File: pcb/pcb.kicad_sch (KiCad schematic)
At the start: 0 parts

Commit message: worked on buttons design
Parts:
- added CH1: choc_v1_SW_HS, PCM_marbastlib-choc:SW_choc_v1_HS_CPG135001S30_1u, symbol PCM_marbastlib-choc:choc_v1_SW_HS_CPG135001S30
- added D1: 1N4148, PCM_Diode_THT_AKL:D_DO-35_SOD27_P7.62mm_Horizontal, symbol PCM_Diode_AKL:1N4148
- added J1: PINHD_1x5_Female, PCM_4ms_Connector:Pins_1x05_2.54mm_TH, symbol PCM_SL_Pin_Headers:PINHD_1x5_Female
- added LED1: choc_SK6812MINI-E, PCM_marbastlib-choc:LED_choc_6028R, symbol PCM_marbastlib-choc:choc_SK6812MINI-E
- added R1: 500, Resistor_THT:R_Axial_DIN0207_L6.3mm_D2.5mm_P10.16mm_Horizontal, symbol PCM_SL_Resistors:Resistor
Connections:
- new net: LED1.2 (DOUT), R1.1
- new net: J1.5, R1.2
- new net: D1.1 (K), J1.2
- new net: CH1.1, D1.2 (A)
- new net: CH1.2, J1.1, LED1.1 (VDD)
- new net: J1.3, LED1.4 (VSS)
- new net: J1.4, LED1.3 (DIN)

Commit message: topshefl work
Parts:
- R1: footprint Resistor_THT:R_Axial_DIN0207_L6.3mm_D2.5mm_P10.16mm_Horizontal -> PCM_4ms_Resistor:R_0603
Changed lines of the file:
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@@
 			)
 		)
-		(property "Footprint" "Resistor_THT:R_Axial_DIN0207_L6.3mm_D2.5mm_P10.16mm_Horizontal"
+		(property "Footprint" "PCM_4ms_Resistor:R_0603"
 			(at 109.601 59.182 0)
 			(effects

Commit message: huh
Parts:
- removed D1: 1N4148, PCM_Diode_THT_AKL:D_DO-35_SOD27_P7.62mm_Horizontal, symbol PCM_Diode_AKL:1N4148
- removed J1: PINHD_1x5_Female, PCM_4ms_Connector:Pins_1x05_2.54mm_TH, symbol PCM_SL_Pin_Headers:PINHD_1x5_Female
- removed LED1: choc_SK6812MINI-E, PCM_marbastlib-choc:LED_choc_6028R, symbol PCM_marbastlib-choc:choc_SK6812MINI-E
- removed R1: 500, PCM_4ms_Resistor:R_0603, symbol PCM_SL_Resistors:Resistor

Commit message: some schematic changes
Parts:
- added C1: 10uF, PCM_Capacitor_SMD_Handsoldering_AKL:C_0805_2012Metric, symbol PCM_Capacitor_AKL:C_0402
- added C2, C4, C5: 100uF, PCM_Capacitor_SMD_Handsoldering_AKL:C_0805_2012Metric, symbol PCM_Capacitor_AKL:C_0402
- added C3: 1uF, PCM_Capacitor_SMD_Handsoldering_AKL:C_0805_2012Metric, symbol PCM_Capacitor_AKL:C_0402
- added IC1: LD1117-3.3V-SOT223, 4ms_Package_SOT:SOT223, symbol PCM_4ms_Regulator:LD1117-3.3V-SOT223
- added J1: Input, PCM_SparkFun-Connector:JST_1x08_P1.25mm_Locking_Horizontal_SMD, symbol PCM_SparkFun-Connector:Conn_01x08_JST_P1.25mm_Locking_Horizontal_SMD
- added J2: Output, PCM_SparkFun-Connector:JST_1x08_P1.25mm_Locking_Horizontal_SMD, symbol PCM_SparkFun-Connector:Conn_01x08_JST_P1.25mm_Locking_Horizontal_SMD
- added J3: PinHeader_01x05_P2.54mm_Horizontal_SMD, PCM_fab:PinHeader_01x05_P2.54mm_Horizontal_SMD, symbol PCM_fab:PinHeader_01x05_P2.54mm_Horizontal_SMD
- added JMP_BTN1, JMP_BTN2, JMP_BTN3, JMP_BTN4, JMP_BTN5, JMP_BTN6, JMP_BTN7, JMP_BTN8: ~, PCM_SparkFun-Jumper:Jumper_2_NO_NoSilk, symbol PCM_SparkFun-Jumper:SolderJumper_2_Open_No_Silk
- added R1: 10k, PCM_4ms_LED:LED_3mm_C1A2_Polarity_Indicator, symbol PCM_Resistor_US_AKL:R_0805
- added R2, R3: 22, PCM_Resistor_SMD_AKL:R_0805_2012Metric, symbol PCM_Resistor_US_AKL:R_0805
- added SW1: Push_Button, Button_Switch_THT:SW_PUSH_6mm, symbol PCM_SL_Devices:Push_Button
- added U1: ~, symbol mycustomsymbols:STM32F042K6
- added USB1: HRO-TYPE-C-31-M-12, extern:HRO-TYPE-C-31-M-12-HandSoldering, symbol Type-C:HRO-TYPE-C-31-M-12
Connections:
- net +3.3V: now reaches CH1.1
- net +3.3V: now also C1.2, C2.2, C4.2, C5.2, IC1.2 (OUT), J1.1 (Pin_1), J2.1 (Pin_1), J3.5 (Pin_5), SW1.2, U1.1 (VDD), U1.17 (VDDIO2), U1.5 (VDDA)
- net at CH1.2: now also JMP_BTN1.1 (A), JMP_BTN2.2 (B), JMP_BTN3.2 (B), JMP_BTN4.2 (B), JMP_BTN5.2 (B), JMP_BTN6.2 (B), JMP_BTN7.2 (B), JMP_BTN8.2 (B)
- new net: R2.2, U1.22 (PA12)
- new net: R1.2, SW1.1, U1.31 (PB8-BOOT0)
- new net: R3.2, U1.21 (PA11)
- new net 5V: C3.1, IC1.3 (IN)
- new net BTN1: JMP_BTN1.2 (B), U1.6 (PA0)
- new net BTN2: J1.2 (Pin_2), J2.2 (Pin_2), JMP_BTN2.1 (A), U1.7 (PA1)
- new net BTN3: J1.3 (Pin_3), J2.3 (Pin_3), JMP_BTN3.1 (A), U1.8 (PA2)
- new net BTN4: J1.4 (Pin_4), J2.4 (Pin_4), JMP_BTN4.1 (A), U1.9 (PA3)
- new net BTN5: J1.5 (Pin_5), J2.5 (Pin_5), JMP_BTN5.1 (A), U1.10 (PA4)
- new net BTN6: J1.6 (Pin_6), J2.6 (Pin_6), JMP_BTN6.1 (A), U1.11 (PA5)
- new net BTN7: J1.7 (Pin_7), J2.7 (Pin_7), JMP_BTN7.1 (A), U1.12 (PA6)
- new net BTN8: J1.8 (Pin_8), J2.8 (Pin_8), JMP_BTN8.1 (A), U1.13 (PA7)
- new net DM: R3.1, USB1.5 (DN2), USB1.7 (DN1)
- new net DP: R2.1, USB1.6 (DP1), USB1.8 (DP2)
- new net GND: C1.1, C2.1, C3.2, C4.1, C5.1, IC1.1 (ADJ), J3.4 (Pin_4), R1.1, U1.16 (VSS), U1.32 (VSS)
- new net RST: J3.1 (Pin_1), U1.4 (NRST)
- new net SWCLK: J3.3 (Pin_3), U1.24 (PA14)
- new net SWDIO: J3.2 (Pin_2), U1.23 (PA13)
- no-connect marks 0 -> 13
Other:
- moved on the sheet: CH1

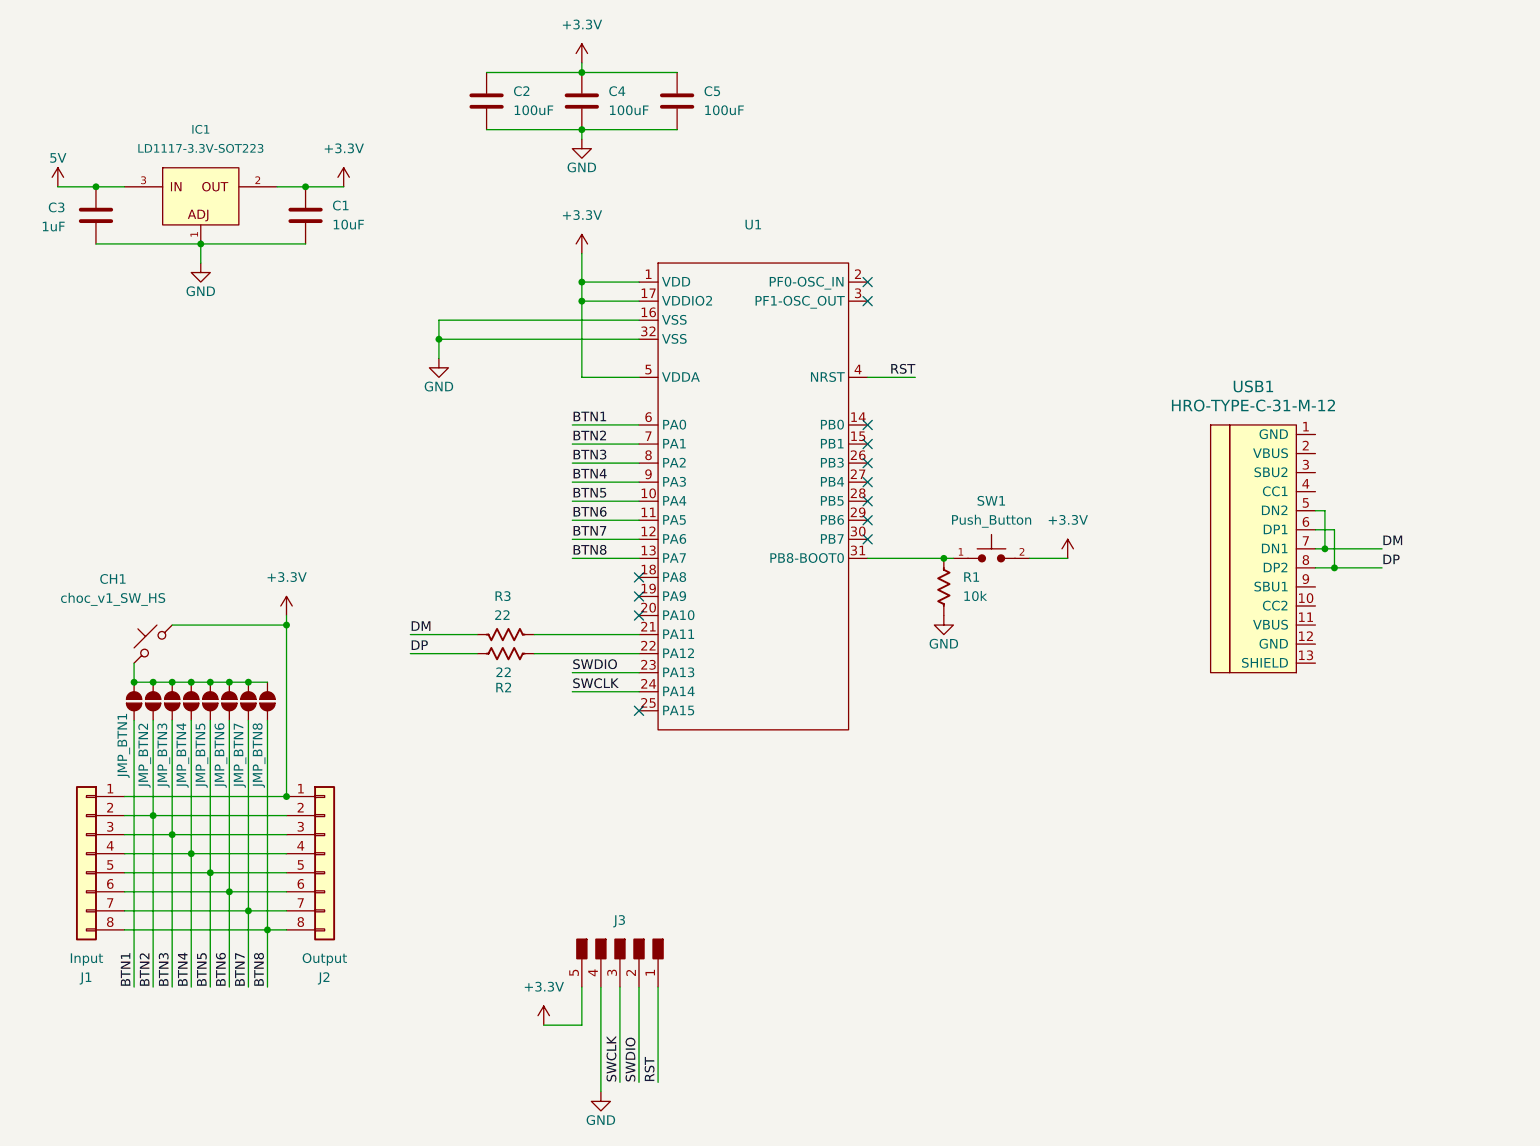
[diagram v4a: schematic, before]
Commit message: making a curved pcb was a mistake, why did i angled this
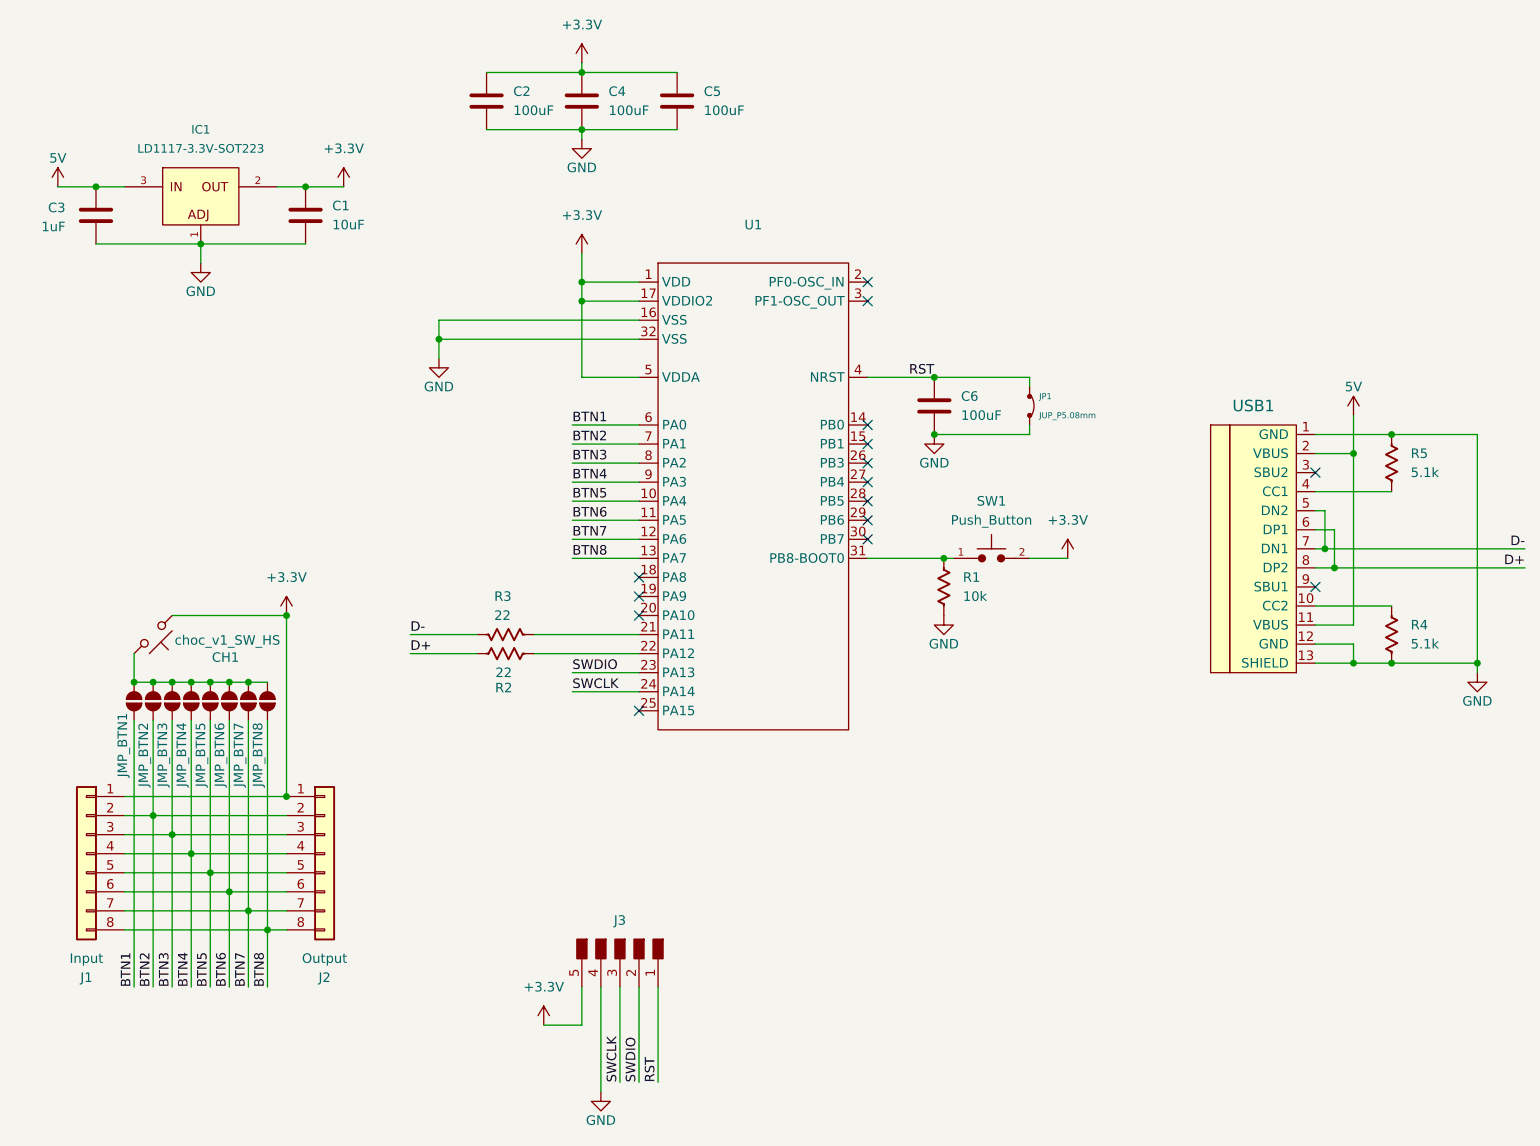
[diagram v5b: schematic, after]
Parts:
- added C6: 100uF, PCM_Capacitor_SMD_Handsoldering_AKL:C_0805_2012Metric, symbol PCM_Capacitor_AKL:C_0402
- added JP1: JUP_P5.08mm, PCM_SL_Jumpers:JUP_P5.08mm, symbol PCM_SL_Jumpers_THT:JUP_P5.08mm
- added R4, R5: 5.1k, PCM_Resistor_SMD_AKL:R_0805_2012Metric, symbol PCM_Resistor_US_AKL:R_0805
- IC1: footprint 4ms_Package_SOT:SOT223 -> PCM_4ms_Package_SOT:SOT223
- J1, J2: footprint PCM_SparkFun-Connector:JST_1x08_P1.25mm_Locking_Horizontal_SMD -> PCM_SparkFun-Connector:1x08_P2.54mm
- R1: footprint PCM_4ms_LED:LED_3mm_C1A2_Polarity_Indicator -> PCM_Resistor_SMD_AKL:R_0805_2012Metric
- U1: footprint (none) -> PCM_Package_QFP_AKL:LQFP-36_7x7mm_P0.65mm
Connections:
- net +3.3V: now also CH1.2; no longer CH1.1
- net 5V: now also USB1.11 (VBUS), USB1.2 (VBUS)
- net GND: now also USB1.1 (GND), USB1.12 (GND), USB1.13 (SHIELD), C6.1, JP1.2, R4.2, R5.1
- net RST: now also C6.2, JP1.1
- net at JMP_BTN1.1 (A), JMP_BTN2.2 (B), JMP_BTN3.2 (B)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: now also CH1.1; no longer CH1.2
- net at USB1.10 (CC2): now also R4.1
- net at USB1.4 (CC1): now also R5.2
- net DM renamed D-
- net DP renamed D+
- no-connect marks 13 -> 15
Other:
- moved on the sheet: CH1

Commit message: pcb drc factoring pending
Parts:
- J3: footprint PCM_fab:PinHeader_01x05_P2.54mm_Horizontal_SMD -> PCM_fab:PinHeader_01x05_P2.54mm_Vertical_THT_D1.4mm
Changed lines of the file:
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@@
 			)
 		)
-		(property "Footprint" "PCM_fab:PinHeader_01x05_P2.54mm_Horizontal_SMD"
+		(property "Footprint" "PCM_fab:PinHeader_01x05_P2.54mm_Vertical_THT_D1.4mm"
 			(at 105.41 146.05 0)
 			(effects

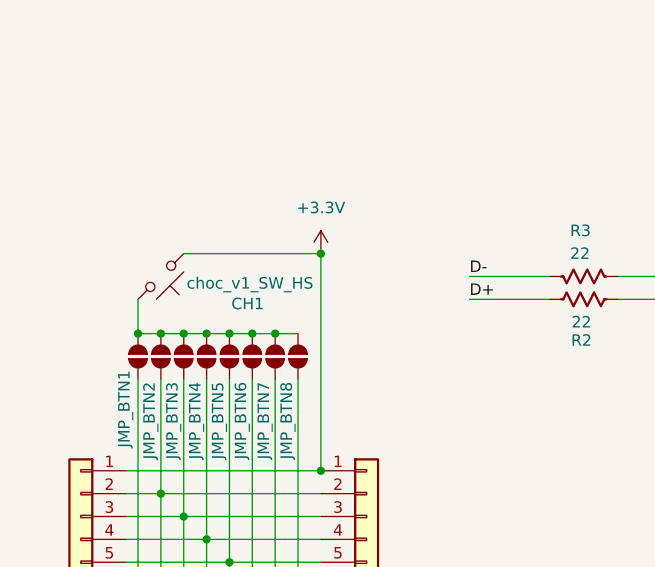
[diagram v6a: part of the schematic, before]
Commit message: drc resolved pcb ordered
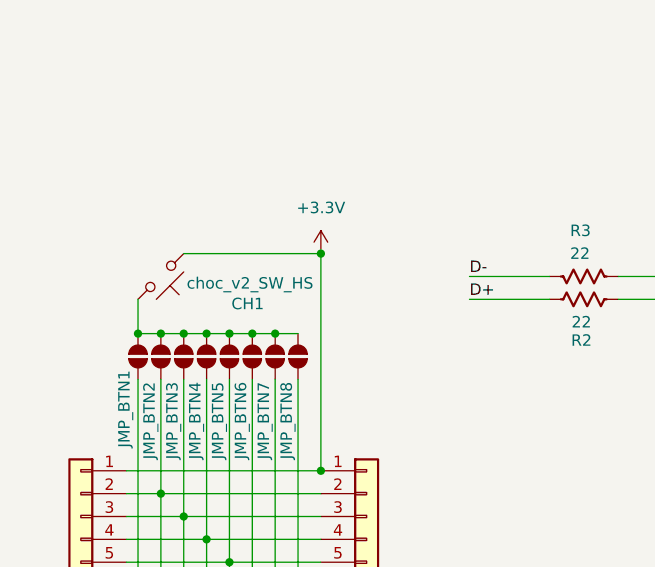
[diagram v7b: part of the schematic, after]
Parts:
- CH1: value choc_v1_SW_HS -> choc_v2_SW_HS
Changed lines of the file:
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@@
 			)
 		)
-		(property "Value" "choc_v1_SW_HS"
+		(property "Value" "choc_v2_SW_HS"
 			(at 53.086 104.902 0)
 			(effects
